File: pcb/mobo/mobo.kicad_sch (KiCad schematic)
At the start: 67 parts, among them J1 ISP, J2 PEEL_MOTOR, J3 DRIVE_MOTOR, J4 SW1, J5 SPRING_FINGERS, J6 SW2, J8 USART1, U1 ATmega328P-A, U2 ATmega328P-M, U4 AP1117-50, U5 MC34063AD, U6 SP308xE, U7 DRV8837, U8 DRV8837, Y1 16MHz

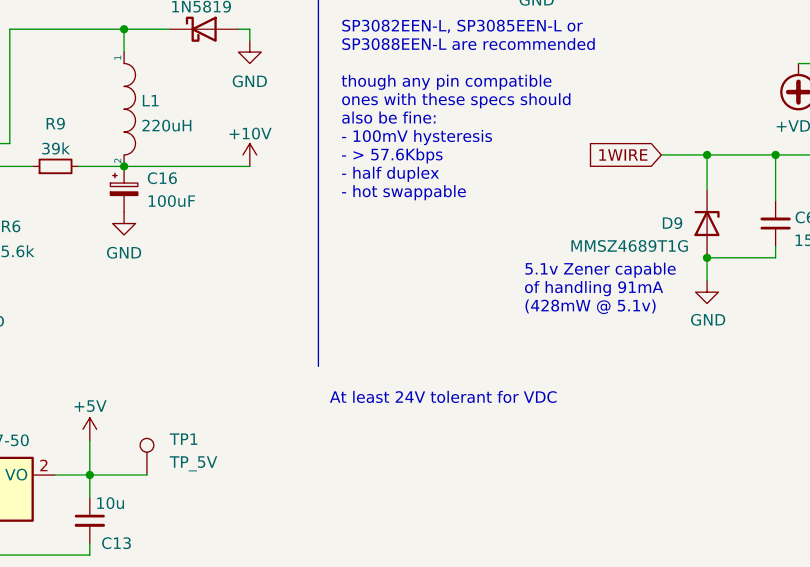
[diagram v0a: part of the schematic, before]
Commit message: Add decoupling cap for RS-485 transceiver, Set edge clearance to 0.2mm
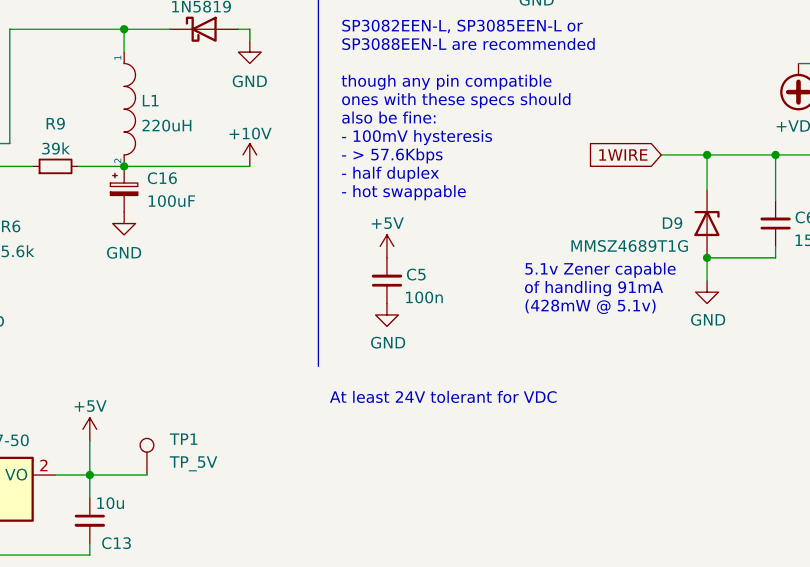
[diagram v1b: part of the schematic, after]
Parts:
- added C5: 100n, Capacitor_SMD:C_0805_2012Metric, symbol Device:C_Small
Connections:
- net +5V: now also C5.2
- net GND: now also C5.1
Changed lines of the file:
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@@
+    )
+  )
+  (symbol (lib_id "power:GND") (at 185.42 158.75 0) (unit 1)
+    (in_bom yes) (on_board yes) (dnp no)
+    (property "Reference" "#PWR023" (at 185.42 165.1 0)
+      (effects (font (size 1.27 1.27)) hide)
+    )
+    (property "Value" "GND" (at 185.547 163.1442 0)
+      (effects (font (size 1.27 1.27)))
+    )
+    (property "Footprint" "" (at 185.42 158.75 0)
+      (effects (font (size 1.27 1.27)) hide)
+    )
+    (property "Datasheet" "" (at 185.42 158.75 0)
+      (effects (font (size 1.27 1.27)) hide)
+    )
+    (pin "1")
+    (instances
+      (project "mobo"
+        (path "/e502d1d5-04b0-4d4b-b5c3-8c52d09668e7"
+          (reference "#PWR023") (unit 1)
+        )
+      )
     )
   )
@@
         (path "/e502d1d5-04b0-4d4b-b5c3-8c52d09668e7"
           (reference "#PWR0130") (unit 1)
+        )
+      )
+    )
+  )
+  (symbol (lib_id "Device:C_Small") (at 185.42 156.21 180) (unit 1)
+    (in_bom yes) (on_board yes) (dnp no)
+    (property "Reference" "C5" (at 189.865 155.575 0)
+      (effects (font (size 1.27 1.27)) (justify left))
+    )
+    (property "Value" "100n" (at 191.77 158.115 0)
+      (effects (font (size 1.27 1.27)) (justify left))
+    )
+    (property "Footprint" "Capacitor_SMD:C_0805_2012Metric" (at 185.42 156.21 0)
+      (effects (font (size 1.27 1.27)) hide)
+    )
+    (property "Datasheet" "~" (at 185.42 156.21 0)
+      (effects (font (size 1.27 1.27)) hide)
+    )
+    (property "JLCPCB" "C49678" (at 185.42 156.21 0)
+      (effects (font (size 1.27 1.27)) hide)
+    )
+    (property "LCSC" "C476766" (at 185.42 156.21 0)
+      (effects (font (size 1.27 1.27)) hide)
+    )
+    (pin "1")
+    (pin "2")
+    (instances
+      (project "mobo"
+        (path "/e502d1d5-04b0-4d4b-b5c3-8c52d09668e7"
+          (reference "C5") (unit 1)
         )
       )
@@
         )
       )
+    )
+  )
+  (symbol (lib_id "power:+5V") (at 185.42 153.67 0) (unit 1)
+    (in_bom yes) (on_board yes) (dnp no)
+    (property "Reference" "#PWR022" (at 185.42 157.48 0)
+      (effects (font (size 1.27 1.27)) hide)
+    )
+    (property "Value" "+5V" (at 185.42 149.86 0)
+      (effects (font (size 1.27 1.27)))
+    )
+    (property "Footprint" "" (at 185.42 153.67 0)
+      (effects (font (size 1.27 1.27)) hide)
+    )
+    (property "Datasheet" "" (at 185.42 153.67 0)
+      (effects (font (size 1.27 1.27)) hide)
+    )
+    (pin "1")
+    (instances
+      (project "mobo"
+        (path "/e502d1d5-04b0-4d4b-b5c3-8c52d09668e7"
+          (reference "#PWR022") (unit 1)
+        )
+      )

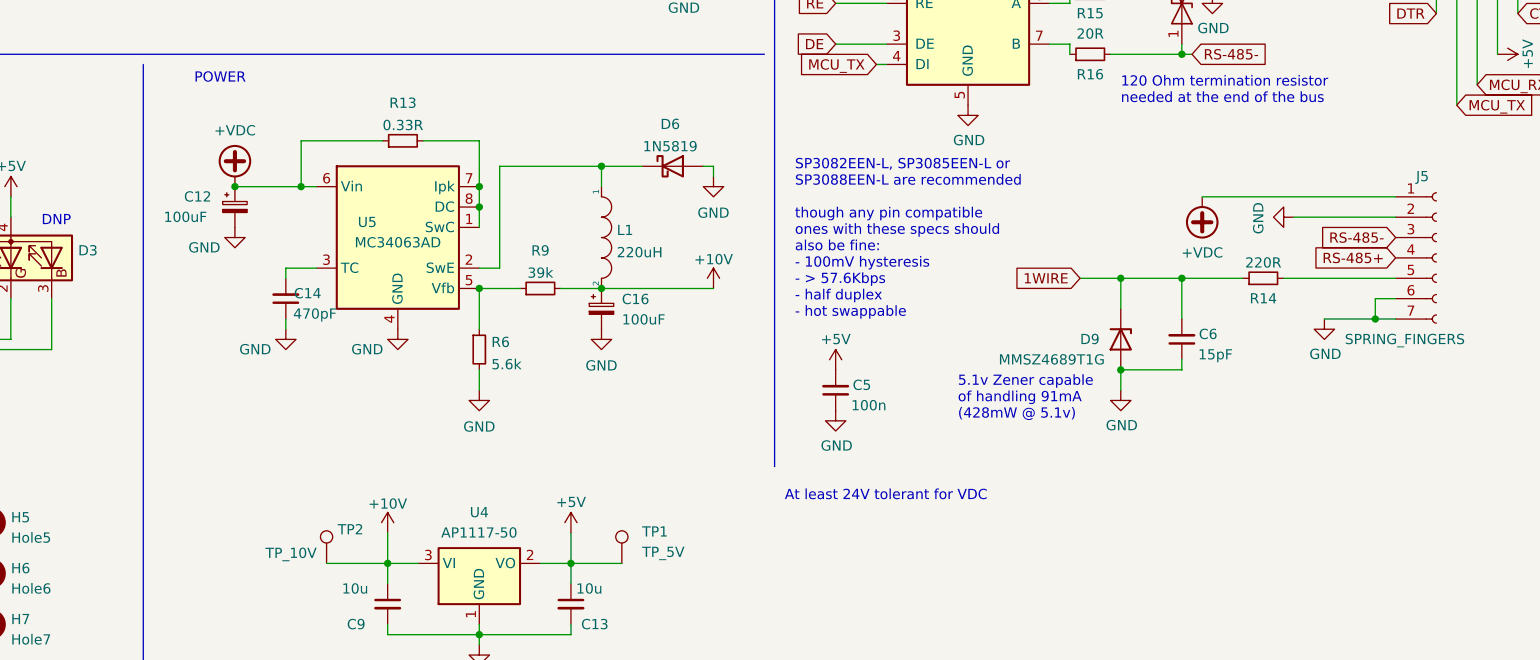
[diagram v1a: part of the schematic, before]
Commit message: Add diode for reverse polarity protection, Add SMPS bypass jumper
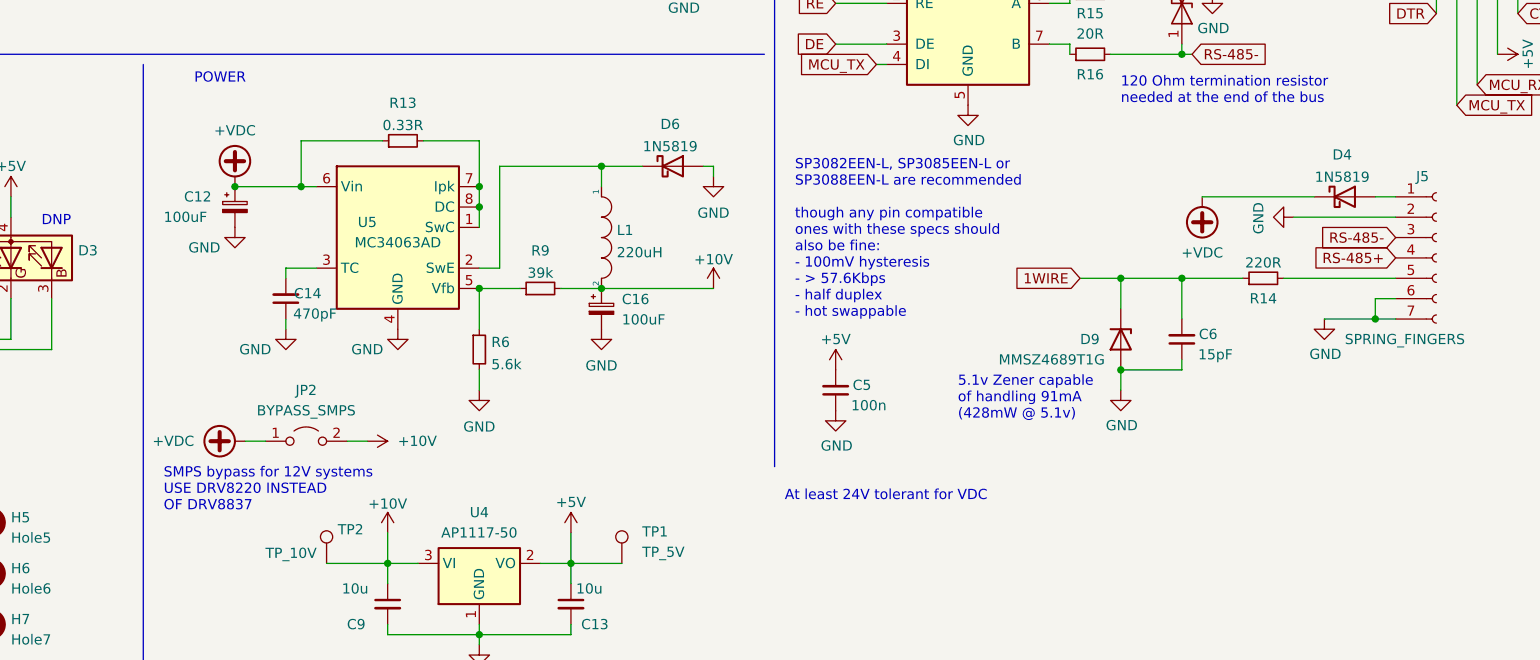
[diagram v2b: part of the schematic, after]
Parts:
- added D4: 1N5819, Diode_SMD:D_SOD-123, symbol Diode:1N5819
- added JP2: BYPASS_SMPS, Jumper:SolderJumper-2_P1.3mm_Open_RoundedPad1.0x1.5mm, symbol Jumper:Jumper_2_Open
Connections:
- net +10V: now also JP2.2 (B)
- net +VDC: now also D4.1 (K), JP2.1 (A); no longer J5.1 (Pin_1)
- new net: D4.2 (A), J5.1 (Pin_1)
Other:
- note added: "SMPS bypass for 12V systems USE DRV8220 INSTEAD OF DRV8837"
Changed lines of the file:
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@@
+    (stroke (width 0) (type default))
+  )
+  (wire (pts (xy 231.14 132.08) (xy 245.11 132.08))
     (stroke (width 0) (type default))
   )
@@
     (stroke (width 0) (type default))
   )
-  (wire (pts (xy 231.14 132.08) (xy 255.27 132.08))
-    (stroke (width 0) (type default))
-  )
   (wire (pts (xy 152.4 186.69) (xy 140.97 186.69))
     (stroke (width 0) (type default))
@@
     (stroke (width 0) (type default))
   )
+  (wire (pts (xy 124.46 162.56) (xy 127 162.56))
+    (stroke (width 0) (type default))
+  )
   (wire (pts (xy 140.97 143.51) (xy 140.97 148.59))
     (stroke (width 0) (type default))
@@
     (stroke (width 0) (type default))
   )
+  (wire (pts (xy 252.73 132.08) (xy 255.27 132.08))
+    (stroke (width 0) (type default))
+  )
   (wire (pts (xy 129.54 177.8) (xy 133.35 177.8))
     (stroke (width 0) (type default))
@@
     (stroke (width 0) (type default))
   )
+  (wire (pts (xy 111.76 162.56) (xy 114.3 162.56))
+    (stroke (width 0) (type default))
+  )
   (wire (pts (xy 43.18 21.59) (xy 43.18 24.13))
     (stroke (width 0) (type default))
@@
   (wire (pts (xy 185.42 113.03) (xy 191.77 113.03))
     (stroke (width 0) (type default))
+  )
+  (text "SMPS bypass for 12V systems\nUSE DRV8220 INSTEAD\nOF DRV8837\n"
+    (at 101.6 171.45 0)
+    (effects (font (size 1.27 1.27)) (justify left bottom))
   )
   (text "I/O" (at 13.97 118.11 0)
@@
         (path "/e502d1d5-04b0-4d4b-b5c3-8c52d09668e7"
           (reference "#PWR0117") (unit 1)
+        )
+      )
+    )
+  )
+  (symbol (lib_id "Jumper:Jumper_2_Open") (at 119.38 162.56 0) (unit 1)
+    (in_bom yes) (on_board yes) (dnp no)
+    (property "Reference" "JP2" (at 119.38 156.21 0)
+      (effects (font (size 1.27 1.27)))
+    )
+    (property "Value" "BYPASS_SMPS" (at 119.38 158.75 0)
+      (effects (font (size 1.27 1.27)))
+    )
+    (property "Footprint" "Jumper:SolderJumper-2_P1.3mm_Open_RoundedPad1.0x1.5mm" (at 119.38 162.56 0)
+      (effects (font (size 1.27 1.27)) hide)
+    )
+    (property "Datasheet" "~" (at 119.38 162.56 0)
+      (effects (font (size 1.27 1.27)) hide)
+    )
+    (pin "1")
+    (pin "2")
+    (instances
+      (project "mobo"
+        (path "/e502d1d5-04b0-4d4b-b5c3-8c52d09668e7"
+          (reference "JP2") (unit 1)
         )
       )
@@
     )
   )
+  (symbol (lib_name "+VDC_1") (lib_id "power:+VDC") (at 111.76 162.56 90) (unit 1)
+    (in_bom yes) (on_board yes) (dnp no)
+    (property "Reference" "#PWR024" (at 114.3 162.56 0)
+      (effects (font (size 1.27 1.27)) hide)
+    )
+    (property "Value" "+VDC" (at 105.41 162.56 90)
+      (effects (font (size 1.27 1.27)) (justify left))
+    )
+    (property "Footprint" "" (at 111.76 162.56 0)
+      (effects (font (size 1.27 1.27)) hide)
+    )
+    (property "Datasheet" "" (at 111.76 162.56 0)
+      (effects (font (size 1.27 1.27)) hide)
+    )
+    (pin "1")
+    (instances
+      (project "mobo"
+        (path "/e502d1d5-04b0-4d4b-b5c3-8c52d09668e7"
+          (reference "#PWR024") (unit 1)
+        )
+      )
+    )
+  )
   (symbol (lib_id "power:GND") (at 116.84 148.59 0) (unit 1)
     (in_bom yes) (on_board yes) (dnp no)
@@
         (path "/e502d1d5-04b0-4d4b-b5c3-8c52d09668e7"
           (reference "TP8") (unit 1)
+        )
+      )
+    )
+  )
+  (symbol (lib_id "power:+10V") (at 127 162.56 270) (unit 1)
+    (in_bom yes) (on_board yes) (dnp no)
+    (property "Reference" "#PWR025" (at 123.19 162.56 0)
+      (effects (font (size 1.27 1.27)) hide)
+    )
+    (property "Value" "+10V" (at 130.81 162.56 90)
+      (effects (font (size 1.27 1.27)) (justify left))
+    )
+    (property "Footprint" "" (at 127 162.56 0)
+      (effects (font (size 1.27 1.27)) hide)
+    )
+    (property "Datasheet" "" (at 127 162.56 0)
+      (effects (font (size 1.27 1.27)) hide)
+    )
+    (pin "1")
+    (instances
+      (project "mobo"
+        (path "/e502d1d5-04b0-4d4b-b5c3-8c52d09668e7"
+          (reference "#PWR025") (unit 1)
         )
       )
@@
         )
       )
+    )
+  )
+  (symbol (lib_id "Diode:1N5819") (at 248.92 132.08 0) (unit 1)
+    (in_bom yes) (on_board yes) (dnp no) (fields_autoplaced)
+    (property "Reference" "D4" (at 248.6025 126.8435 0)
+      (effects (font (size 1.27 1.27)))
+    )
+    (property "Value" "1N5819" (at 248.6025 129.6186 0)
+      (effects (font (size 1.27 1.27)))
+    )
+    (property "Footprint" "Diode_SMD:D_SOD-123" (at 248.92 136.525 0)
+      (effects (font (size 1.27 1.27)) hide)
+    )
+    (property "Datasheet" "http://www.vishay.com/docs/88525/1n5817.pdf" (at 248.92 132.08 0)
+      (effects (font (size 1.27 1.27)) hide)
+    )
+    (pin "1")
+    (pin "2")
+    (instances
+      (project "mobo"
+        (path "/e502d1d5-04b0-4d4b-b5c3-8c52d09668e7"
+          (reference "D4") (unit 1)
+        )
+      )

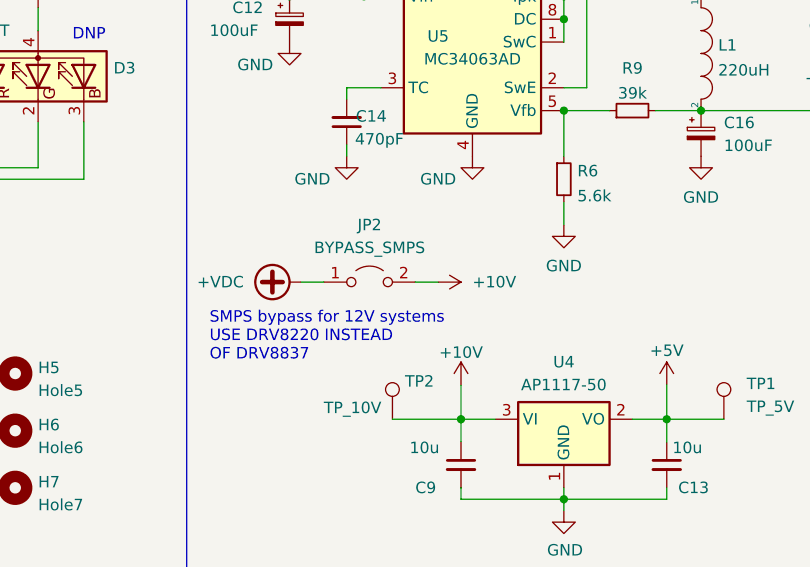
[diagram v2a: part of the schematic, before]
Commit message: Replace bypass jumper with 0R resistor
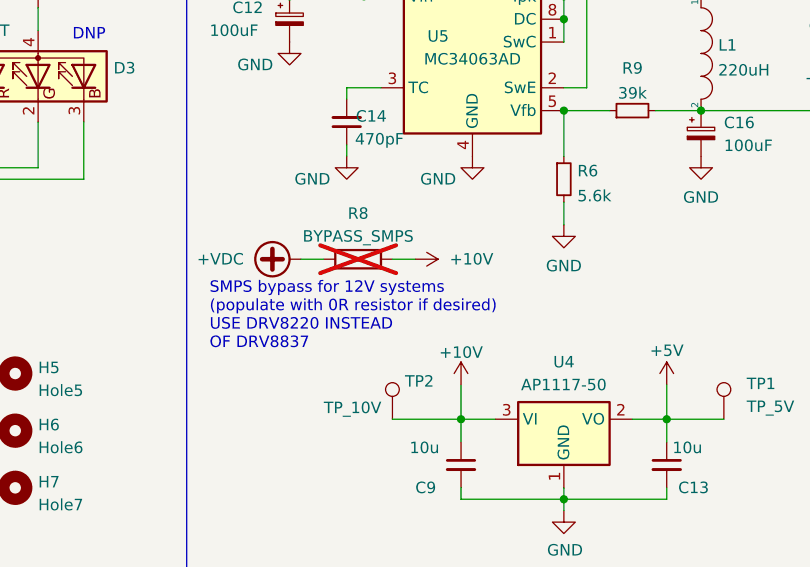
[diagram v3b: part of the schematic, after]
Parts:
- removed JP2: BYPASS_SMPS, Jumper:SolderJumper-2_P1.3mm_Open_RoundedPad1.0x1.5mm, symbol Jumper:Jumper_2_Open
- added R8: BYPASS_SMPS, Resistor_SMD:R_0805_2012Metric, symbol Device:R
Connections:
- net +10V: now also R8.2
- net +VDC: now also R8.1
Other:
- note added: "SMPS bypass for 12V systems (populate with 0R resistor if desired) USE DRV8220 INSTEAD OF DRV8837"
- note removed: "SMPS bypass for 12V systems USE DRV8220 INSTEAD OF DRV8837"
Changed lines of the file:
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@@
     (stroke (width 0) (type default))
   )
-  (wire (pts (xy 124.46 162.56) (xy 127 162.56))
+  (wire (pts (xy 121.92 160.02) (xy 124.46 160.02))
     (stroke (width 0) (type default))
   )
@@
     (stroke (width 0) (type default))
   )
-  (wire (pts (xy 111.76 162.56) (xy 114.3 162.56))
+  (wire (pts (xy 111.76 160.02) (xy 114.3 160.02))
     (stroke (width 0) (type default))
   )
@@
     (stroke (width 0) (type default))
   )
-  (text "SMPS bypass for 12V systems\nUSE DRV8220 INSTEAD\nOF DRV8837\n"
-    (at 101.6 171.45 0)
+  (text "SMPS bypass for 12V systems\n(populate with 0R resistor if desired)\nUSE DRV8220 INSTEAD\nOF DRV8837\n"
+    (at 101.6 170.18 0)
     (effects (font (size 1.27 1.27)) (justify left bottom))
   )
@@
         (path "/e502d1d5-04b0-4d4b-b5c3-8c52d09668e7"
           (reference "#PWR0117") (unit 1)
-        )
-      )
-    )
-  )
-  (symbol (lib_id "Jumper:Jumper_2_Open") (at 119.38 162.56 0) (unit 1)
-    (in_bom yes) (on_board yes) (dnp no)
-    (property "Reference" "JP2" (at 119.38 156.21 0)
-      (effects (font (size 1.27 1.27)))
-    )
-    (property "Value" "BYPASS_SMPS" (at 119.38 158.75 0)
-      (effects (font (size 1.27 1.27)))
-    )
-    (property "Footprint" "Jumper:SolderJumper-2_P1.3mm_Open_RoundedPad1.0x1.5mm" (at 119.38 162.56 0)
-      (effects (font (size 1.27 1.27)) hide)
-    )
-    (property "Datasheet" "~" (at 119.38 162.56 0)
-      (effects (font (size 1.27 1.27)) hide)
-    )
-    (pin "1")
-    (pin "2")
-    (instances
-      (project "mobo"
-        (path "/e502d1d5-04b0-4d4b-b5c3-8c52d09668e7"
-          (reference "JP2") (unit 1)
         )
       )
@@
     )
   )
-  (symbol (lib_name "+VDC_1") (lib_id "power:+VDC") (at 111.76 162.56 90) (unit 1)
-    (in_bom yes) (on_board yes) (dnp no)
-    (property "Reference" "#PWR024" (at 114.3 162.56 0)
-      (effects (font (size 1.27 1.27)) hide)
-    )
-    (property "Value" "+VDC" (at 105.41 162.56 90)
-      (effects (font (size 1.27 1.27)) (justify left))
-    )
-    (property "Footprint" "" (at 111.76 162.56 0)
-      (effects (font (size 1.27 1.27)) hide)
-    )
-    (property "Datasheet" "" (at 111.76 162.56 0)
+  (symbol (lib_name "+VDC_1") (lib_id "power:+VDC") (at 111.76 160.02 90) (unit 1)
+    (in_bom yes) (on_board yes) (dnp no)
+    (property "Reference" "#PWR024" (at 114.3 160.02 0)
+      (effects (font (size 1.27 1.27)) hide)
+    )
+    (property "Value" "+VDC" (at 105.41 160.02 90)
+      (effects (font (size 1.27 1.27)) (justify left))
+    )
+    (property "Footprint" "" (at 111.76 160.02 0)
+      (effects (font (size 1.27 1.27)) hide)
+    )
+    (property "Datasheet" "" (at 111.76 160.02 0)
       (effects (font (size 1.27 1.27)) hide)
     )
@@
     )
   )
-  (symbol (lib_id "power:+10V") (at 127 162.56 270) (unit 1)
-    (in_bom yes) (on_board yes) (dnp no)
-    (property "Reference" "#PWR025" (at 123.19 162.56 0)
-      (effects (font (size 1.27 1.27)) hide)
-    )
-    (property "Value" "+10V" (at 130.81 162.56 90)
-      (effects (font (size 1.27 1.27)) (justify left))
-    )
-    (property "Footprint" "" (at 127 162.56 0)
-      (effects (font (size 1.27 1.27)) hide)
-    )
-    (property "Datasheet" "" (at 127 162.56 0)
+  (symbol (lib_id "power:+10V") (at 124.46 160.02 270) (unit 1)
+    (in_bom yes) (on_board yes) (dnp no)
+    (property "Reference" "#PWR025" (at 120.65 160.02 0)
+      (effects (font (size 1.27 1.27)) hide)
+    )
+    (property "Value" "+10V" (at 128.27 160.02 90)
+      (effects (font (size 1.27 1.27)) (justify left))
+    )
+    (property "Footprint" "" (at 124.46 160.02 0)
+      (effects (font (size 1.27 1.27)) hide)
+    )
+    (property "Datasheet" "" (at 124.46 160.02 0)
       (effects (font (size 1.27 1.27)) hide)
     )
@@
         )
       )
+    )
+  )
+  (symbol (lib_id "Device:R") (at 118.11 160.02 90) (unit 1)
+    (in_bom yes) (on_board yes) (dnp yes) (fields_autoplaced)
+    (property "Reference" "R8" (at 118.11 154.94 90)
+      (effects (font (size 1.27 1.27)))
+    )
+    (property "Value" "BYPASS_SMPS" (at 118.11 157.48 90)
+      (effects (font (size 1.27 1.27)))
+    )
+    (property "Footprint" "Resistor_SMD:R_0805_2012Metric" (at 118.11 161.798 90)
+      (effects (font (size 1.27 1.27)) hide)
+    )
+    (property "Datasheet" "~" (at 118.11 160.02 0)
+      (effects (font (size 1.27 1.27)) hide)
+    )
+    (pin "1")
+    (pin "2")
+    (instances
+      (project "mobo"
+        (path "/e502d1d5-04b0-4d4b-b5c3-8c52d09668e7"
+          (reference "R8") (unit 1)
+        )
+      )
